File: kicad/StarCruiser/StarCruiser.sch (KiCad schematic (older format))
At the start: 43 parts, among them Q10 2N4126, Q11 2N4124, Q12 2N4127, Q13 2N4124, Q6 2N4124, Q7 2N4134, Q8 2N4124, Q9 2N4124, U2 LM741

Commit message: Star Cruiser: first corrections, thanks to Andrew
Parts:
- removed R23: 2.5K, symbol R
- added R23: 2.5K, symbol POT
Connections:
- wire segments 84 -> 83
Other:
- moved on the sheet: R22
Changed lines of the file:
@@
-	-1   0    0    1
-$EndComp
-$Comp
-L R R23
-U 1 1 559FE735
-P 5900 850
-F 0 "R23" H 6050 850 50  0000 C CNN
-F 1 "2.5K" V 5900 850 50  0000 C CNN
-F 2 "" V 5830 850 30  0000 C CNN
-F 3 "" H 5900 850 30  0000 C CNN
-	1    5900 850
 	-1   0    0    1
 $EndComp
@@
 L R R22
 U 1 1 559FE7FA
-P 6250 600
-F 0 "R22" V 6330 600 50  0000 C CNN
-F 1 "0.47K" V 6250 600 50  0000 C CNN
-F 2 "" V 6180 600 30  0000 C CNN
-F 3 "" H 6250 600 30  0000 C CNN
-	1    6250 600
+P 6250 500
+F 0 "R22" V 6330 500 50  0000 C CNN
+F 1 "0.47K" V 6250 500 50  0000 C CNN
+F 2 "" V 6180 500 30  0000 C CNN
+F 3 "" H 6250 500 30  0000 C CNN
+	1    6250 500
 	0    1    1    0
 $EndComp
@@
 L +12V #PWR?
 U 1 1 559FE894
-P 6600 600
-F 0 "#PWR?" H 6600 450 50  0001 C CNN
-F 1 "+12V" V 6700 650 50  0000 C CNN
-F 2 "" H 6600 600 60  0000 C CNN
-F 3 "" H 6600 600 60  0000 C CNN
-	1    6600 600
+P 6600 500
+F 0 "#PWR?" H 6600 350 50  0001 C CNN
+F 1 "+12V" V 6700 550 50  0000 C CNN
+F 2 "" H 6600 500 60  0000 C CNN
+F 3 "" H 6600 500 60  0000 C CNN
+	1    6600 500
 	0    1    1    0
 $EndComp
@@
 F 3 "" H 6000 1500 50  0000 L CNN
 	1    6000 1500
-	-1   0    0    1
+	-1   0    0    -1
 $EndComp
 $Comp
@@
 	8250 1300 8250 1200
 Wire Wire Line
-	6400 600  6600 600
-Wire Wire Line
-	6100 600  5900 600
-Wire Wire Line
-	5900 600  5900 700
-Wire Wire Line
-	5950 850  8250 850
-Wire Wire Line
-	6050 750  6050 950
+	6400 500  6600 500
+Wire Wire Line
+	6100 500  5900 500
+Wire Wire Line
+	6050 600  6050 950
 Wire Wire Line
 	5900 1000 5900 1300
@@
 Wire Wire Line
 	5900 1100 6200 1100
-Connection ~ 6200 850
-Wire Wire Line
-	6200 850  6200 1050
+Connection ~ 6200 750
+Wire Wire Line
+	6200 750  6200 1050
 Wire Wire Line
 	6200 1050 4650 1050
@@
 	7100 3400 7650 3400
 Wire Wire Line
-	8250 850  8250 1000
+	8250 750  8250 1000
 Connection ~ 8250 1700
 Wire Wire Line
@@
 F 3 "" H 4650 4050 50  0000 L CNN
 	1    4650 4050
-	1    0    0    -1
+	1    0    0    1
 $EndComp
 Wire Wire Line
@@
 Text Notes 2450 4950 0    30   ~ 0
 What's this chip? 315 - 3F?\nOsso
+$Comp
+L POT R23
+U 1 1 559FC58B
+P 5900 750
+F 0 "R23" V 5800 600 50  0000 C CNN
+F 1 "2.5K" H 5900 750 50  0000 C CNN
+F 2 "" H 5900 750 60  0000 C CNN
+F 3 "" H 5900 750 60  0000 C CNN
+	1    5900 750
+	0    1    1    0
+$EndComp
+Wire Wire Line
+	6050 750  8250 750
 $EndSCHEMATC

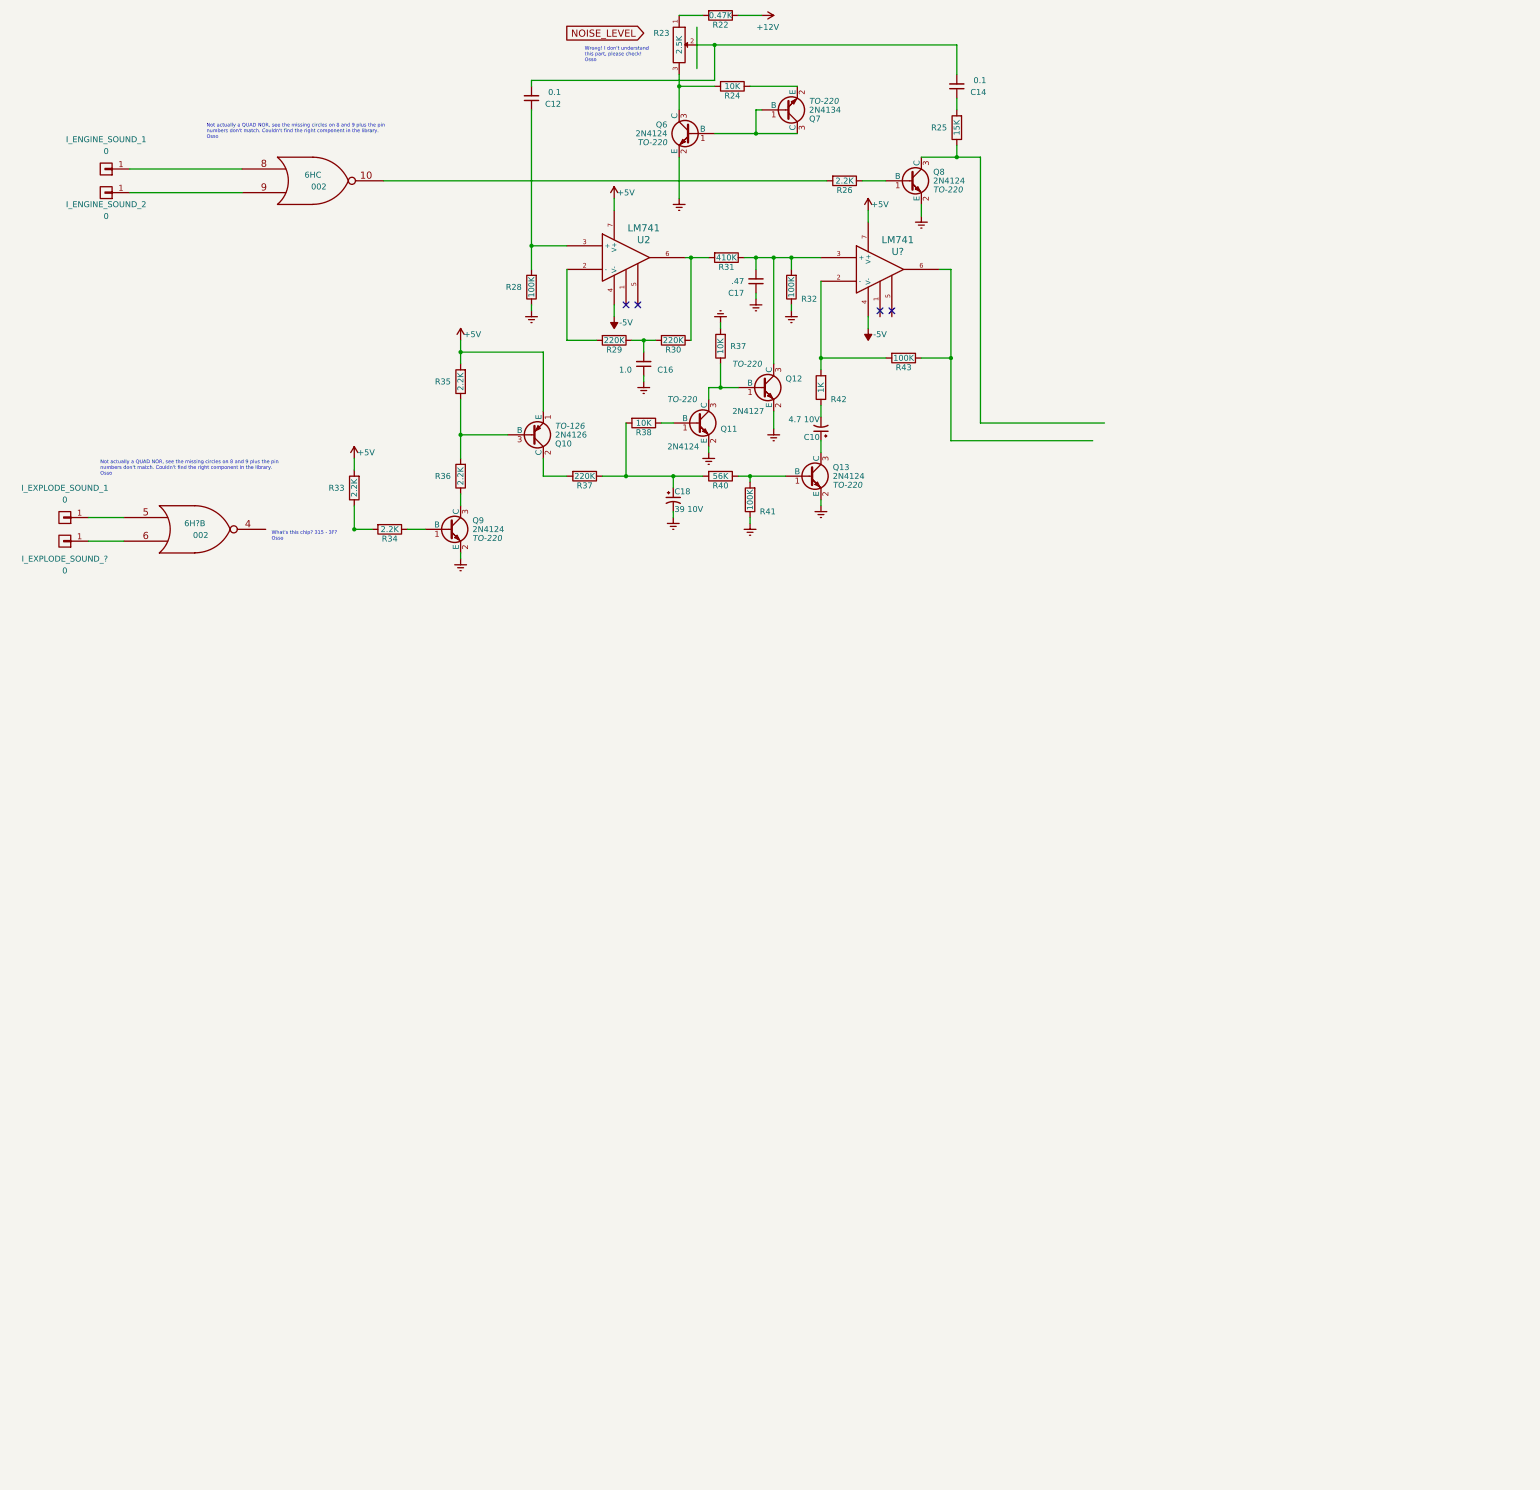
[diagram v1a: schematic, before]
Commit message: Star Cruiser: more WIP, right block missing (LM379)
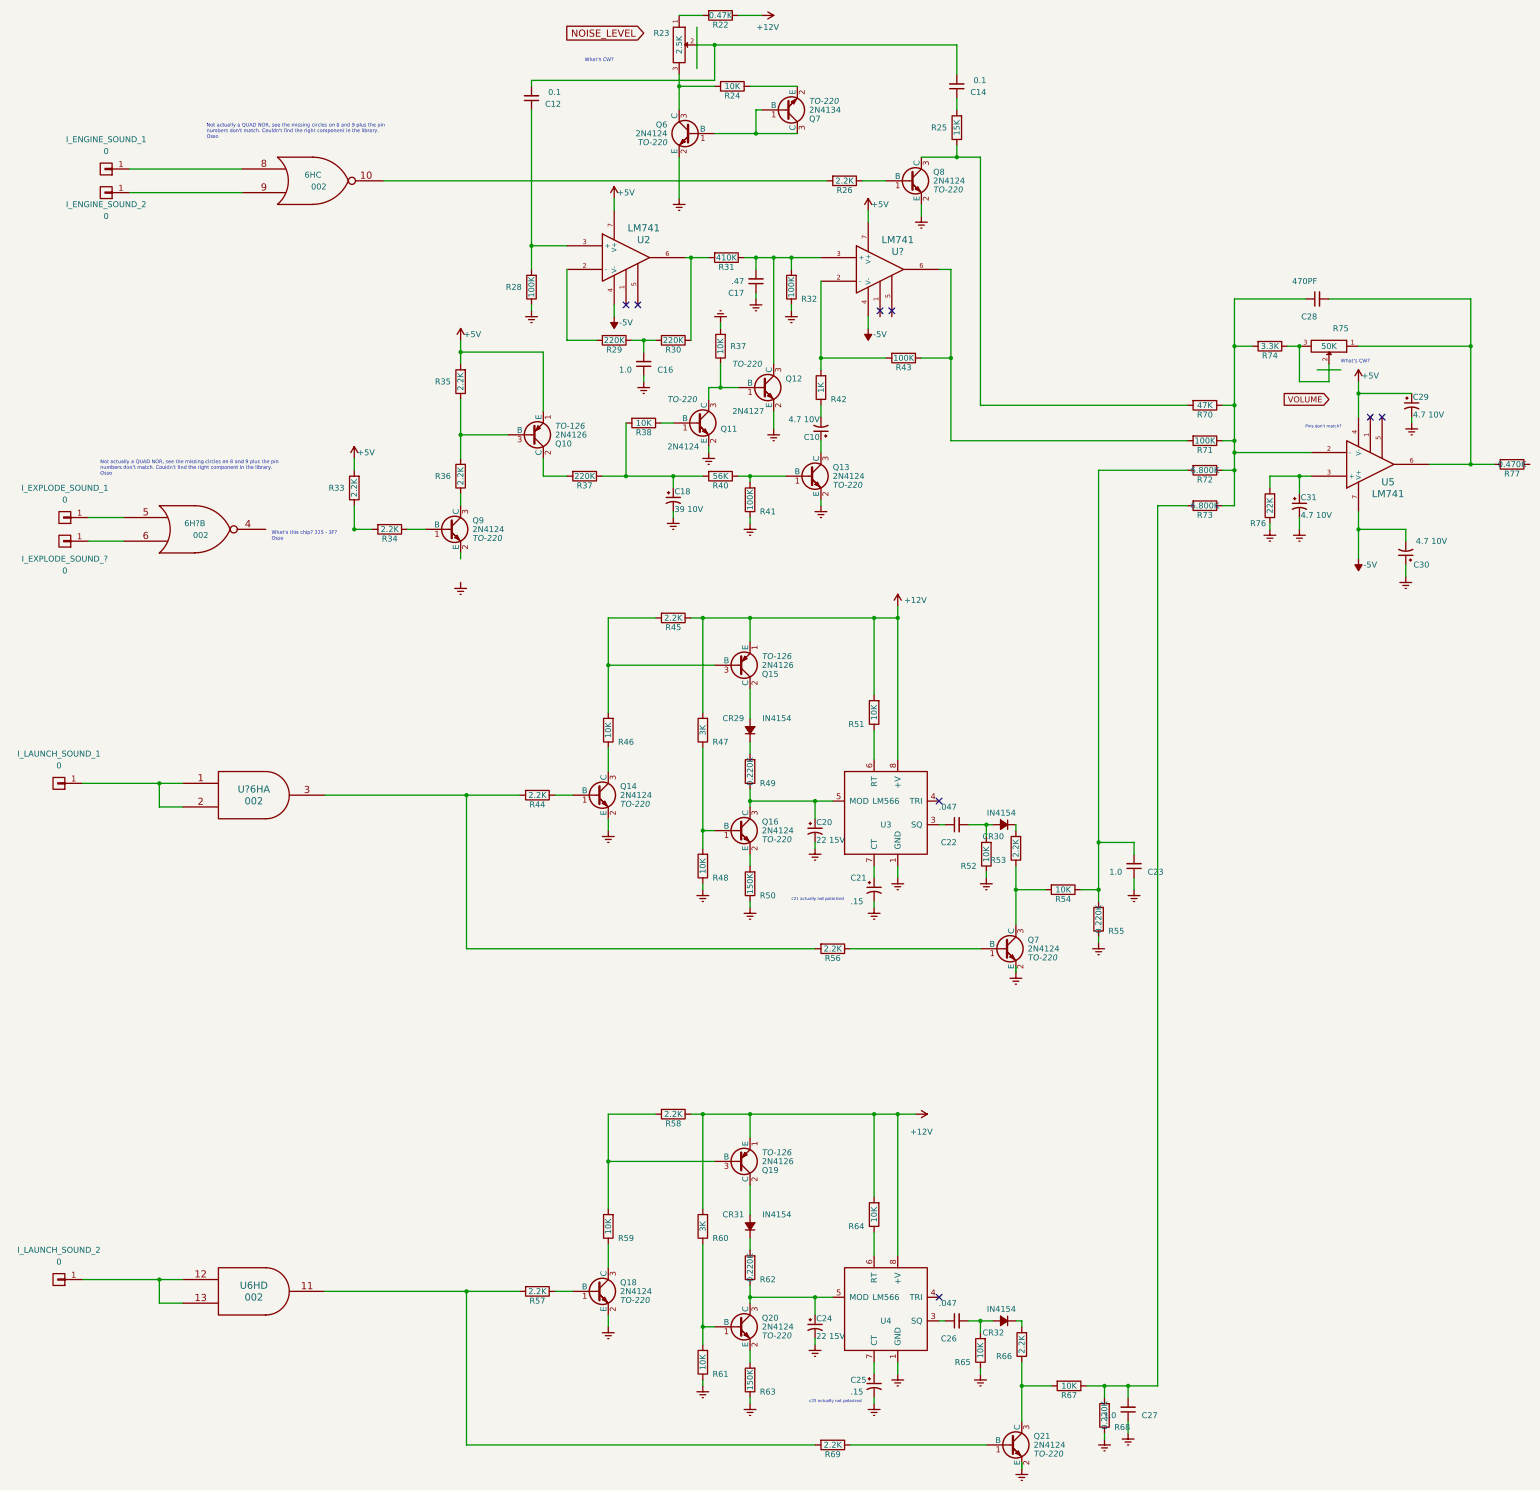
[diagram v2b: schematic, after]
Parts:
- added C20, C24: 22 15V, symbol CP1_Small
- added C21, C25: .15, symbol CP1_Small
- added C22, C26: .047, symbol C_Small
- added C23, C27: 1.0, symbol C_Small
- added C28: 470PF, symbol C_Small
- added C29, C30, C31: 4.7 10V, symbol CP1_Small
- added CR29, CR30, CR31, CR32: IN4154, symbol D_Small
- added I_LAUNCH_SOUND_1, I_LAUNCH_SOUND_2: 0, symbol CONN_01X01
- added Q14, Q16, Q18, Q20, Q21, Q7: 2N4124, TO-220, symbol 2SC1945
- added Q15, Q19: 2N4126, TO-126, symbol 2SB631
- added R44, R45, R53, R56, R57, R58, R66, R69: 2.2K, symbol R
- added R46, R48, R51, R52, R54, R59, R61, R64, R65, R67: 10K, symbol R
- added R47, R60: 3K, symbol R
- added R49, R55, R62, R68: 0.220K, symbol R
- added R50, R63: 150K, symbol R
- added R70: 47K, symbol R
- added R71: 100K, symbol R
- added R72, R73: 6.800K, symbol R
- added R74: 3.3K, symbol R
- added R75: 50K, symbol POT
- added R76: 22K, symbol R
- added R77: 0.470K, symbol R
- added U3, U4: LM566, symbol LM566
- added U5: LM741, symbol LM741
- added U6H, U?6H: 002, symbol 74LS08
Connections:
- net labels added: VOLUME
- wire segments 83 -> 209
- no-connect marks 4 -> 8
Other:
- note added: "Pins don't match?"
- note added: "What's CW?"
- note added: "c21 actually not polarized"
- note added: "c25 actually not polarized"
- note removed: "Wrong! I don't understand\nthis part, please check!\nOsso"
